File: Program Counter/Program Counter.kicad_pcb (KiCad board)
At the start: 2 copper layers, 54 x 56 mm, 50 parts, among them IC1 SN74AHCT16245DGGR, J1 Conn_01x05, J2 Conn_02x15_Odd_Even, J3 Conn_02x15_Odd_Even, U1 74LS161, U2 74LS161, U3 74LS161, U4 74LS161

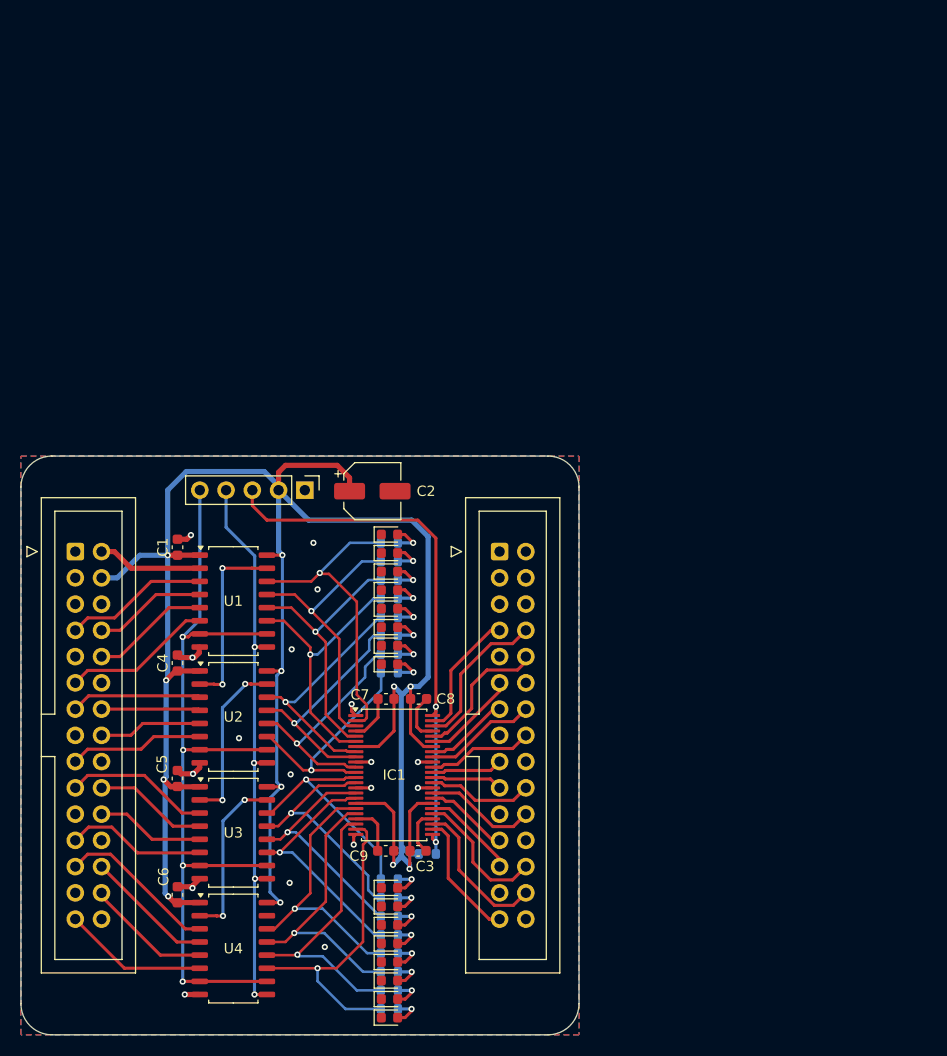
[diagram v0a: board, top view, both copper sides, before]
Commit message: Updated silkscreen and cascade wiring program counter
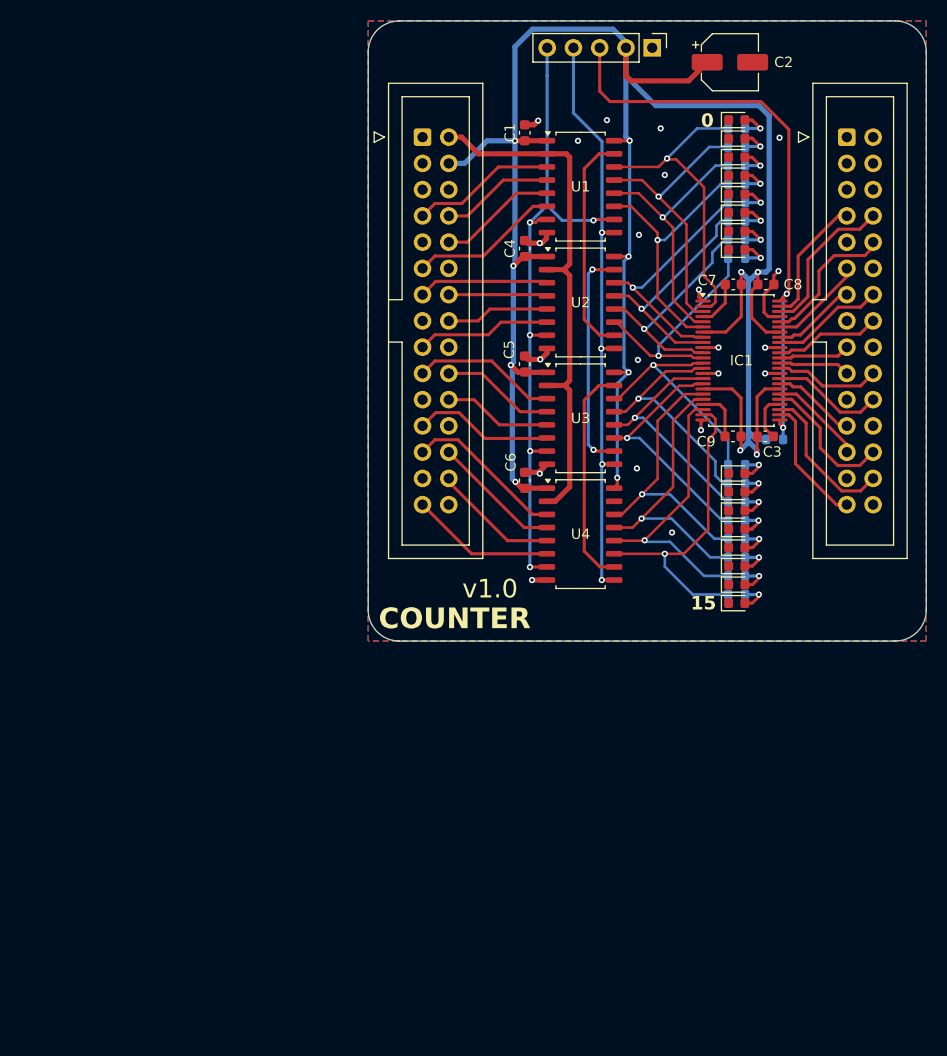
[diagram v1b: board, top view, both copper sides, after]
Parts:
- moved J1 54.4 mm to (140.1, 63.5)
- moved C2 54.0 mm to (147.6, 64.9)
- moved U2 52.3 mm to (133.2, 88.1)
- moved C1 52.3 mm to (127.8, 71.7)
- moved C3 52.3 mm to (151.0, 101.1)
- moved C4 52.3 mm to (127.8, 82.9)
- moved C7 52.3 mm to (147.9, 86.4)
- moved C9 52.3 mm to (147.9, 101.1)
- moved D10 52.3 mm to (148.3, 75.9)
- moved D12 52.3 mm to (148.3, 83.0)
- moved D13 52.3 mm to (148.3, 106.5)
- moved D14 52.3 mm to (148.3, 110.1)
- moved D2 52.3 mm to (148.3, 74.1)
- moved D5 52.3 mm to (148.3, 104.7)
- moved D6 52.3 mm to (148.3, 108.3)
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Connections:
- J3 pad 1: /bus_conn1/GND -> GND
- J3 pad 12: /bus_conn1/GND -> GND
- J3 pad 15: /bus_conn1/GND -> GND
- J3 pad 18: /bus_conn1/GND -> GND
- J3 pad 21: /bus_conn1/GND -> GND
- J3 pad 24: /bus_conn1/GND -> GND
- J3 pad 27: /bus_conn1/GND -> GND
- J3 pad 3: /bus_conn1/GND -> GND
- J3 pad 30: /bus_conn1/GND -> GND
- J3 pad 5: /bus_conn1/GND -> GND
- J3 pad 6: /bus_conn1/GND -> GND
- J3 pad 9: /bus_conn1/GND -> GND
- U2 pad 10: /PCE -> Net-(U1-TC)
- U2 pad 2: Net-(U1-TC) -> /CLK
- U3 pad 10: /PCE -> Net-(U2-TC)
- U3 pad 2: Net-(U2-TC) -> /CLK
- U4 pad 10: /PCE -> Net-(U3-TC)
- U4 pad 2: Net-(U3-TC) -> /CLK
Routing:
- net /CLK: track 10.2 -> 51.4 mm
- net /PCE: track 80.8 -> 64.8 mm, vias 4 -> 5
- net Net-(U2-TC): track 16.5 -> 22.1 mm
- net +5V: track 218.6 -> 224.0 mm
- net Net-(U3-TC): track 16.6 -> 21.6 mm, vias 2 -> 0
- net Net-(U1-TC): track 17.7 -> 21.6 mm, vias 2 -> 0
- net /~{PCO}: track 53.1 -> 56.2 mm
- net /~{PCL}: track 54.7 -> 57.4 mm
- net GND: track 38.6 -> 40.1 mm, vias 18 -> 21
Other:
- board size 54 x 56 mm -> 54 x 60 mm
- board text added: "0"
- board text added: "15"
- board text added: "COUNTER"
- board text added: "v1.0"
